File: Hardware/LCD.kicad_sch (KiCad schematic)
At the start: 7 parts, among them U11 PI4IOE5V9535LEX

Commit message: Clean up custom KiCad libraries
- Clean up the directory structure for KiCad custom libraries.
- Fix paths in KiCad schematic and pcb for symbols, footprints, and
3d models for custom libraries.
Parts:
- DS1: footprint Libs:C162BLBSBSW6WN33PAB -> Display:C162BLBSBSW6WN33PAB
- RV5: footprint Libs:PTV09A-4015U-B103 -> Potentiometer:PTV09A-4015U-B103
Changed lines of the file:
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@@
   (title_block
     (title "Musical Doorbell")
-    (date "2022-01-06")
-    (rev "B")
+    (date "2022-01-09")
+    (rev "A")
     (company "Michael Lazernik")
   )
@@
     (property "Reference" "DS1" (id 0) (at 184.15 54.1782 0))
     (property "Value" "C162BLBSBSW6WN33PAB" (id 1) (at 184.15 56.4896 0))
-    (property "Footprint" "Libs:C162BLBSBSW6WN33PAB" (id 2) (at 184.15 99.06 0)
+    (property "Footprint" "Display:C162BLBSBSW6WN33PAB" (id 2) (at 184.15 99.06 0)
       (effects (font (size 1.27 1.27) italic) hide)
     )
@@
       (effects (font (size 1.27 1.27)) (justify right))
     )
-    (property "Footprint" "Libs:PTV09A-4015U-B103" (id 2) (at 199.39 76.2 0)
+    (property "Footprint" "Potentiometer:PTV09A-4015U-B103" (id 2) (at 199.39 76.2 0)
       (effects (font (size 1.27 1.27)) hide)
     )

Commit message: Cleanup custom KiCad libraries
- Delete unneeded/unused files
- Cleanup symbol library files for custom libraries
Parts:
- DS1: symbol C162BLBSBSW6WN33PAB:C162BLBSBSW6WN33PAB -> Doorbell_Display:C162BLBSBSW6WN33PAB
- RV5: symbol PTV09A-4015U-B103:PTV09A-4015U-B103 -> Doorbell_Potentiometer:PTV09A-4015U-B103
- U11: symbol PI4IOE5V9535LEX:PI4IOE5V9535LEX -> Doorbell_IC:PI4IOE5V9535LEX
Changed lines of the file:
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@@
     (effects (font (size 1.27 1.27)) (justify right))
   )
-  (symbol (lib_id "C162BLBSBSW6WN33PAB:C162BLBSBSW6WN33PAB") (at 184.15 76.2 0) (unit 1)
+  (symbol (lib_id "Doorbell_Display:C162BLBSBSW6WN33PAB") (at 184.15 76.2 0) (unit 1)
     (in_bom yes) (on_board yes)
     (property "Reference" "DS1" (id 0) (at 184.15 54.1782 0))
@@
     (pin "9")
   )
-  (symbol (lib_id "PTV09A-4015U-B103:PTV09A-4015U-B103") (at 199.39 76.2 0) (mirror y) (unit 1)
+  (symbol (lib_id "Doorbell_Potentiometer:PTV09A-4015U-B103") (at 199.39 76.2 0) (mirror y) (unit 1)
     (in_bom yes) (on_board yes)
     (property "Reference" "RV5" (id 0) (at 200.914 78.5114 0)
@@
     (pin "1")
   )
-  (symbol (lib_id "PI4IOE5V9535LEX:PI4IOE5V9535LEX") (at 140.97 72.39 0) (unit 1)
+  (symbol (lib_id "Doorbell_IC:PI4IOE5V9535LEX") (at 140.97 72.39 0) (unit 1)
     (in_bom yes) (on_board yes)
     (property "Reference" "U11" (id 0) (at 140.97 46.5582 0))

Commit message: Switch to local libraries for KiCad schematic
- Move all KiCad schematic symbols into local libraries
- Fix KiCad schematic library links to point to local libraries
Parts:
- C36: symbol Device:C_Small -> Doorbell_Capacitor:C_Small
- R32, R33, R34: symbol Device:R_Small -> Doorbell_Resistor:R_Small
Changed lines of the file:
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@@
     (pin "3")
   )
-  (symbol (lib_id "power:GND") (at 199.39 93.98 0) (unit 1)
+  (symbol (lib_id "Doorbell_Power:GND") (at 199.39 93.98 0) (unit 1)
     (in_bom yes) (on_board yes)
     (property "Reference" "#PWR055" (id 0) (at 199.39 100.33 0)
@@
     (pin "9")
   )
-  (symbol (lib_id "power:GND") (at 120.65 93.98 0) (unit 1)
+  (symbol (lib_id "Doorbell_Power:GND") (at 120.65 93.98 0) (unit 1)
     (in_bom yes) (on_board yes)
     (property "Reference" "#PWR054" (id 0) (at 120.65 100.33 0)
@@
     (pin "1")
   )
-  (symbol (lib_id "Device:C_Small") (at 113.03 46.99 0) (unit 1)
+  (symbol (lib_id "Doorbell_Capacitor:C_Small") (at 113.03 46.99 0) (unit 1)
     (in_bom yes) (on_board yes)
     (property "Reference" "C36" (id 0) (at 115.3668 45.8216 0)
@@
     (pin "2")
   )
-  (symbol (lib_id "Device:R_Small") (at 105.41 46.99 0) (unit 1)
+  (symbol (lib_id "Doorbell_Resistor:R_Small") (at 105.41 46.99 0) (unit 1)
     (in_bom yes) (on_board yes)
     (property "Reference" "R34" (id 0) (at 106.9086 45.8216 0)
@@
     (pin "2")
   )
-  (symbol (lib_id "Device:R_Small") (at 99.06 46.99 0) (unit 1)
+  (symbol (lib_id "Doorbell_Resistor:R_Small") (at 99.06 46.99 0) (unit 1)
     (in_bom yes) (on_board yes)
     (property "Reference" "R33" (id 0) (at 100.5586 45.8216 0)
@@
     (pin "2")
   )
-  (symbol (lib_id "Device:R_Small") (at 92.71 46.99 0) (unit 1)
+  (symbol (lib_id "Doorbell_Resistor:R_Small") (at 92.71 46.99 0) (unit 1)
     (in_bom yes) (on_board yes)
     (property "Reference" "R32" (id 0) (at 94.2086 45.8216 0)
@@
     (pin "2")
   )
-  (symbol (lib_id "power:GND") (at 113.03 52.07 0) (unit 1)
+  (symbol (lib_id "Doorbell_Power:GND") (at 113.03 52.07 0) (unit 1)
     (in_bom yes) (on_board yes)
     (property "Reference" "#PWR053" (id 0) (at 113.03 58.42 0)
@@
     (pin "1")
   )
-  (symbol (lib_id "power:GND") (at 115.57 93.98 0) (unit 1)
+  (symbol (lib_id "Doorbell_Power:GND") (at 115.57 93.98 0) (unit 1)
     (in_bom yes) (on_board yes)
     (property "Reference" "#PWR0101" (id 0) (at 115.57 100.33 0)
@@
     (pin "1")
   )
-  (symbol (lib_id "power:PWR_FLAG") (at 120.65 91.44 0) (unit 1)
+  (symbol (lib_id "Doorbell_Power:PWR_FLAG") (at 120.65 91.44 0) (unit 1)
     (in_bom yes) (on_board yes)
     (property "Reference" "#FLG0102" (id 0) (at 120.65 89.535 0)

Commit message: Move KiCad global footprint and 3d models to local
- Move KiCad global footprint and 3d models to local directories
- Reassign footprints in KiCad schematic/PCB from global libraries to
  local libraries
- Reassign global 3d models to local 3d models for KiCad
- Update KiCad PCB with all local footprints
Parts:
- U11: footprint Package_SO:TSSOP-24_4.4x7.8mm_P0.65mm -> IC:TSSOP-24_4.4x7.8mm_P0.65mm
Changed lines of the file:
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@@
     (property "Reference" "U11" (id 0) (at 140.97 46.5582 0))
     (property "Value" "PI4IOE5V9535LEX" (id 1) (at 140.97 48.8696 0))
-    (property "Footprint" "Package_SO:TSSOP-24_4.4x7.8mm_P0.65mm" (id 2) (at 146.05 100.33 0)
+    (property "Footprint" "IC:TSSOP-24_4.4x7.8mm_P0.65mm" (id 2) (at 146.05 100.33 0)
       (effects (font (size 1.27 1.27)) (justify left) hide)
     )

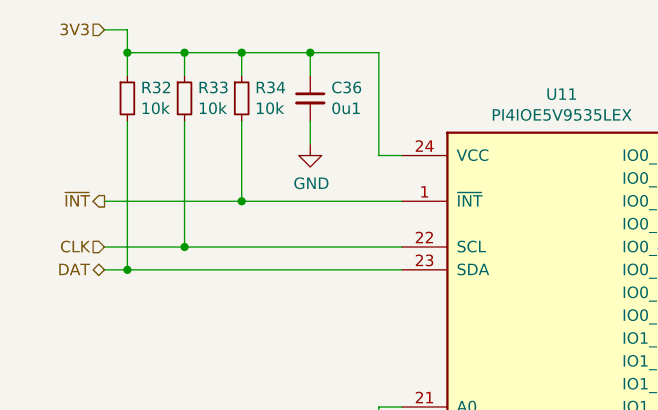
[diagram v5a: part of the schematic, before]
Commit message: Bump to board revision B
- Redesign low battery circuit
	- Replace comparator with PMIC
	- Utilize LED Driver IC
	- Remove unneeded 2.5v voltage reference
- Reroute some signals onto wkup/external interrupt pins
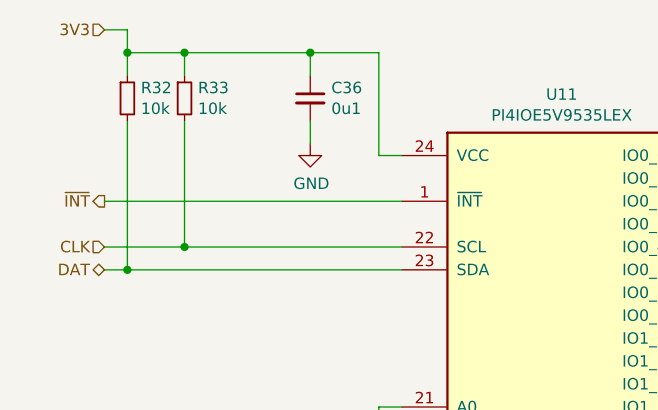
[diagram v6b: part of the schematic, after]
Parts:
- removed R34: 10k, Resistor_SMD:R_0603_1608Metric_Pad0.98x0.95mm_HandSolder, symbol Doorbell_Resistor:R_Small
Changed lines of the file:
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@@
   (title_block
     (title "Musical Doorbell")
-    (date "2022-01-11")
-    (rev "A")
+    (date "2022-02-25")
+    (rev "B")
     (company "Michael Lazernik")
   )
@@
   (junction (at 199.39 60.96) (diameter 0) (color 0 0 0 0)
   )
-  (junction (at 105.41 41.91) (diameter 0) (color 0 0 0 0)
-  )
   (junction (at 99.06 63.5) (diameter 0) (color 0 0 0 0)
   )
   (junction (at 199.39 91.44) (diameter 0) (color 0 0 0 0)
-  )
-  (junction (at 105.41 58.42) (diameter 0) (color 0 0 0 0)
   )
   (junction (at 120.65 91.44) (diameter 0) (color 0 0 0 0)
@@
     (stroke (width 0) (type default) (color 0 0 0 0))
   )
-  (wire (pts (xy 99.06 41.91) (xy 105.41 41.91))
+  (wire (pts (xy 99.06 41.91) (xy 113.03 41.91))
     (stroke (width 0) (type default) (color 0 0 0 0))
   )
@@
     (stroke (width 0) (type default) (color 0 0 0 0))
   )
-  (wire (pts (xy 113.03 41.91) (xy 105.41 41.91))
-    (stroke (width 0) (type default) (color 0 0 0 0))
-  )
-  (wire (pts (xy 90.17 58.42) (xy 105.41 58.42))
-    (stroke (width 0) (type default) (color 0 0 0 0))
-  )
   (wire (pts (xy 120.65 91.44) (xy 120.65 93.98))
     (stroke (width 0) (type default) (color 0 0 0 0))
@@
     (stroke (width 0) (type default) (color 0 0 0 0))
   )
-  (wire (pts (xy 105.41 44.45) (xy 105.41 41.91))
-    (stroke (width 0) (type default) (color 0 0 0 0))
-  )
   (wire (pts (xy 199.39 91.44) (xy 199.39 93.98))
     (stroke (width 0) (type default) (color 0 0 0 0))
   )
-  (wire (pts (xy 105.41 58.42) (xy 123.19 58.42))
+  (wire (pts (xy 90.17 58.42) (xy 123.19 58.42))
     (stroke (width 0) (type default) (color 0 0 0 0))
   )
@@
   )
   (wire (pts (xy 120.65 83.82) (xy 120.65 86.36))
-    (stroke (width 0) (type default) (color 0 0 0 0))
-  )
-  (wire (pts (xy 105.41 49.53) (xy 105.41 58.42))
     (stroke (width 0) (type default) (color 0 0 0 0))
   )
@@
       (effects (font (size 1.27 1.27)) hide)
     )
-    (pin "1")
-    (pin "2")
-  )
-  (symbol (lib_id "Doorbell_Resistor:R_Small") (at 105.41 46.99 0) (unit 1)
-    (in_bom yes) (on_board yes)
-    (property "Reference" "R34" (id 0) (at 106.9086 45.8216 0)
-      (effects (font (size 1.27 1.27)) (justify left))
-    )
-    (property "Value" "10k" (id 1) (at 106.9086 48.133 0)
-      (effects (font (size 1.27 1.27)) (justify left))
-    )
-    (property "Footprint" "Resistor_SMD:R_0603_1608Metric_Pad0.98x0.95mm_HandSolder" (id 2) (at 105.41 46.99 0)
-      (effects (font (size 1.27 1.27)) hide)
-    )
-    (property "Datasheet" "~" (id 3) (at 105.41 46.99 0)
-      (effects (font (size 1.27 1.27)) hide)
-    )
